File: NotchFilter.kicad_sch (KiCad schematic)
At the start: 10 parts, among them U4 LM2904DR

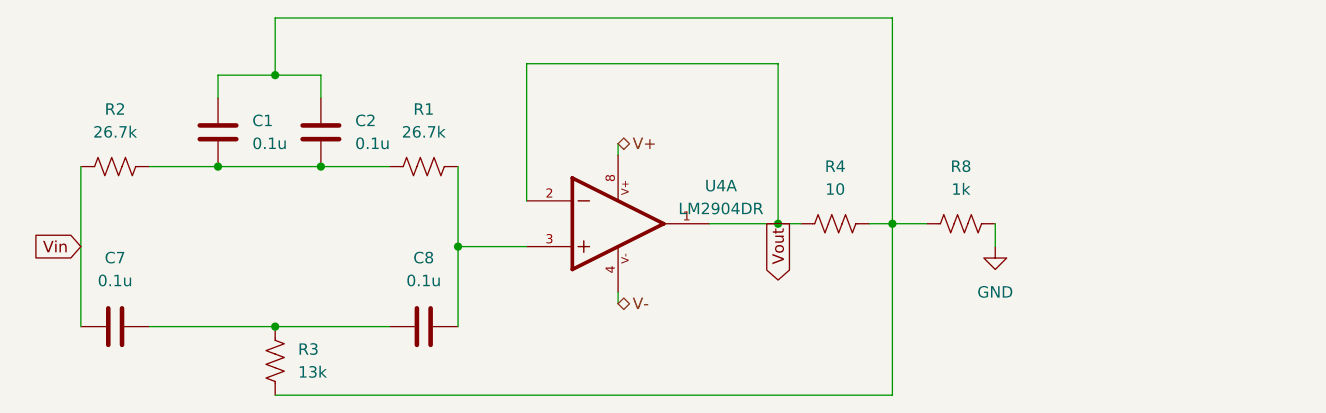
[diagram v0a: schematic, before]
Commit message: swapped lpf and hpf in bandpass filter and added testpoints on various filter circuits
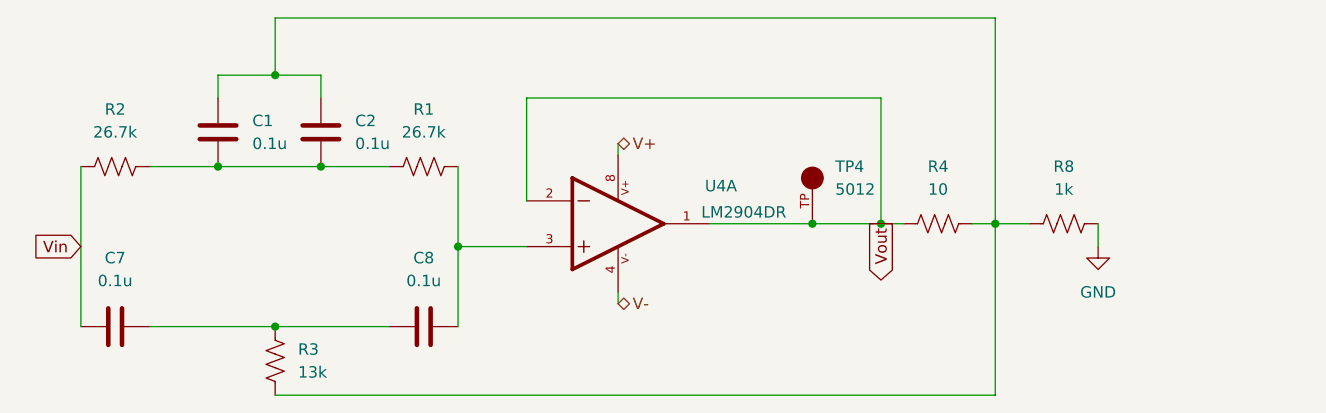
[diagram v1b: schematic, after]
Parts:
- added TP4: 5012, 5012:TP_5012, symbol TP_5012:5012
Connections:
- net Vout: now also TP4.TP
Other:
- moved on the sheet: R4, R8
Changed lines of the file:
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@@
 (kicad_sch (version 20230121) (generator eeschema)
   (paper "A4")
+  (junction (at 209.55 77.47) (diameter 0) (color 0 0 0 0)
+  )
+  (junction (at 162.56 80.01) (diameter 0) (color 0 0 0 0)
+  )
   (junction (at 142.24 60.96) (diameter 0) (color 0 0 0 0)
   )
-  (junction (at 198.12 77.47) (diameter 0) (color 0 0 0 0)
-  )
-  (junction (at 162.56 80.01) (diameter 0) (color 0 0 0 0)
-  )
   (junction (at 135.89 71.12) (diameter 0) (color 0 0 0 0)
   )
-  (junction (at 210.82 77.47) (diameter 0) (color 0 0 0 0)
+  (junction (at 222.25 77.47) (diameter 0) (color 0 0 0 0)
+  )
+  (junction (at 201.93 77.47) (diameter 0) (color 0 0 0 0)
   )
   (junction (at 147.32 71.12) (diameter 0) (color 0 0 0 0)
@@
     (stroke (width 0) (type default))
   )
-  (wire (pts (xy 170.18 59.69) (xy 198.12 59.69))
+  (wire (pts (xy 170.18 63.5) (xy 209.55 63.5))
     (stroke (width 0) (type default))
   )
@@
     (stroke (width 0) (type default))
   )
-  (wire (pts (xy 142.24 96.52) (xy 210.82 96.52))
+  (wire (pts (xy 201.93 77.47) (xy 209.55 77.47))
     (stroke (width 0) (type default))
   )
@@
     (stroke (width 0) (type default))
   )
+  (wire (pts (xy 135.89 60.96) (xy 142.24 60.96))
+    (stroke (width 0) (type default))
+  )
   (wire (pts (xy 162.56 80.01) (xy 162.56 88.9))
     (stroke (width 0) (type default))
   )
+  (wire (pts (xy 170.18 63.5) (xy 170.18 74.93))
+    (stroke (width 0) (type default))
+  )
   (wire (pts (xy 142.24 54.61) (xy 142.24 60.96))
     (stroke (width 0) (type default))
   )
-  (wire (pts (xy 190.5 77.47) (xy 198.12 77.47))
-    (stroke (width 0) (type default))
-  )
   (wire (pts (xy 162.56 71.12) (xy 162.56 80.01))
     (stroke (width 0) (type default))
@@
     (stroke (width 0) (type default))
   )
-  (wire (pts (xy 222.25 77.47) (xy 222.25 80.01))
+  (wire (pts (xy 233.68 77.47) (xy 233.68 80.01))
     (stroke (width 0) (type default))
   )
@@
     (stroke (width 0) (type default))
   )
-  (wire (pts (xy 210.82 77.47) (xy 214.63 77.47))
-    (stroke (width 0) (type default))
-  )
-  (wire (pts (xy 170.18 74.93) (xy 170.18 59.69))
-    (stroke (width 0) (type default))
-  )
-  (wire (pts (xy 210.82 54.61) (xy 142.24 54.61))
+  (wire (pts (xy 222.25 77.47) (xy 226.06 77.47))
+    (stroke (width 0) (type default))
+  )
+  (wire (pts (xy 222.25 54.61) (xy 142.24 54.61))
     (stroke (width 0) (type default))
   )
@@
     (stroke (width 0) (type default))
   )
+  (wire (pts (xy 190.5 77.47) (xy 201.93 77.47))
+    (stroke (width 0) (type default))
+  )
   (wire (pts (xy 147.32 71.12) (xy 154.94 71.12))
     (stroke (width 0) (type default))
   )
-  (wire (pts (xy 135.89 60.96) (xy 142.24 60.96))
-    (stroke (width 0) (type default))
-  )
-  (wire (pts (xy 208.28 77.47) (xy 210.82 77.47))
+  (wire (pts (xy 219.71 77.47) (xy 222.25 77.47))
+    (stroke (width 0) (type default))
+  )
+  (wire (pts (xy 222.25 77.47) (xy 222.25 54.61))
     (stroke (width 0) (type default))
   )
@@
     (stroke (width 0) (type default))
   )
-  (wire (pts (xy 210.82 77.47) (xy 210.82 54.61))
-    (stroke (width 0) (type default))
-  )
   (wire (pts (xy 180.34 85.09) (xy 180.34 86.36))
     (stroke (width 0) (type default))
   )
-  (wire (pts (xy 198.12 77.47) (xy 200.66 77.47))
-    (stroke (width 0) (type default))
-  )
-  (wire (pts (xy 210.82 77.47) (xy 210.82 96.52))
-    (stroke (width 0) (type default))
-  )
-  (wire (pts (xy 198.12 59.69) (xy 198.12 77.47))
+  (wire (pts (xy 142.24 96.52) (xy 222.25 96.52))
+    (stroke (width 0) (type default))
+  )
+  (wire (pts (xy 209.55 77.47) (xy 212.09 77.47))
+    (stroke (width 0) (type default))
+  )
+  (wire (pts (xy 222.25 77.47) (xy 222.25 96.52))
+    (stroke (width 0) (type default))
+  )
+  (wire (pts (xy 209.55 63.5) (xy 209.55 77.47))
     (stroke (width 0) (type default))
   )
@@
     (stroke (width 0) (type default))
   )
-  (global_label "Vout" (shape output) (at 198.12 77.47 270) (fields_autoplaced)
+  (global_label "Vout" (shape output) (at 209.55 77.47 270) (fields_autoplaced)
     (effects (font (size 1.27 1.27)) (justify right))
-    (property "Intersheetrefs" "${INTERSHEET_REFS}" (at 198.12 84.5675 90)
+    (property "Intersheetrefs" "${INTERSHEET_REFS}" (at 209.55 84.5675 90)
       (effects (font (size 1.27 1.27)) (justify right) hide)
     )
@@
   )
   (symbol (lib_id "LM2904DR:LM2904DR") (at 180.34 77.47 0) (unit 1)
-    (in_bom yes) (on_board yes) (dnp no) (fields_autoplaced)
+    (in_bom yes) (on_board yes) (dnp no)
     (property "Reference" "U4" (at 191.77 73.2791 0)
       (effects (font (size 1.27 1.27)))
     )
-    (property "Value" "LM2904DR" (at 191.77 75.8191 0)
+    (property "Value" "LM2904DR" (at 194.31 76.2 0)
       (effects (font (size 1.27 1.27)))
     )
@@
     )
   )
-  (symbol (lib_id "power:GND") (at 222.25 80.01 0) (unit 1)
-    (in_bom yes) (on_board yes) (dnp no) (fields_autoplaced)
-    (property "Reference" "#PWR02" (at 222.25 86.36 0)
-      (effects (font (size 1.27 1.27)) hide)
-    )
-    (property "Value" "GND" (at 222.25 85.09 0)
-      (effects (font (size 1.27 1.27)))
-    )
-    (property "Footprint" "" (at 222.25 80.01 0)
-      (effects (font (size 1.27 1.27)) hide)
-    )
-    (property "Datasheet" "" (at 222.25 80.01 0)
+  (symbol (lib_id "power:GND") (at 233.68 80.01 0) (unit 1)
+    (in_bom yes) (on_board yes) (dnp no) (fields_autoplaced)
+    (property "Reference" "#PWR02" (at 233.68 86.36 0)
+      (effects (font (size 1.27 1.27)) hide)
+    )
+    (property "Value" "GND" (at 233.68 85.09 0)
+      (effects (font (size 1.27 1.27)))
+    )
+    (property "Footprint" "" (at 233.68 80.01 0)
+      (effects (font (size 1.27 1.27)) hide)
+    )
+    (property "Datasheet" "" (at 233.68 80.01 0)
       (effects (font (size 1.27 1.27)) hide)
     )
@@
         (path "/c6167f6f-8a8c-40a1-9c06-7f0e8ea44639/7fb3b184-acaf-47e3-98f1-99223ca2f08b"
           (reference "C7") (unit 1)
+        )
+      )
+    )
+  )
+  (symbol (lib_id "TP_5012:5012") (at 201.93 72.39 90) (unit 1)
+    (in_bom yes) (on_board yes) (dnp no) (fields_autoplaced)
+    (property "Reference" "TP4" (at 204.47 71.12 90)
+      (effects (font (size 1.27 1.27)) (justify right))
+    )
+    (property "Value" "5012" (at 204.47 73.66 90)
+      (effects (font (size 1.27 1.27)) (justify right))
+    )
+    (property "Footprint" "5012:TP_5012" (at 201.93 72.39 0)
+      (effects (font (size 1.27 1.27)) (justify bottom) hide)
+    )
+    (property "Datasheet" "" (at 201.93 72.39 0)
+      (effects (font (size 1.27 1.27)) hide)
+    )
+    (property "PARTREV" "F" (at 201.93 72.39 0)
+      (effects (font (size 1.27 1.27)) (justify bottom) hide)
+    )
+    (property "SNAPEDA_PN" "5010" (at 201.93 72.39 0)
+      (effects (font (size 1.27 1.27)) (justify bottom) hide)
+    )
+    (property "MANUFACTURER" "Keystone Electronics" (at 201.93 72.39 0)
+      (effects (font (size 1.27 1.27)) (justify bottom) hide)
+    )
+    (property "MAXIMUM_PACKAGE_HEIGHT" "8.13 mm" (at 201.93 72.39 0)
+      (effects (font (size 1.27 1.27)) (justify bottom) hide)
+    )
+    (property "STANDARD" "Manufacturer Recommendations" (at 201.93 72.39 0)
+      (effects (font (size 1.27 1.27)) (justify bottom) hide)
+    )
+    (pin "TP")
+    (instances
+      (project "TR_EMG"
+        (path "/c6167f6f-8a8c-40a1-9c06-7f0e8ea44639/7fb3b184-acaf-47e3-98f1-99223ca2f08b"
+          (reference "TP4") (unit 1)
         )
       )
@@
     )
   )
-  (symbol (lib_id "Device:R_US") (at 218.44 77.47 270) (unit 1)
-    (in_bom yes) (on_board yes) (dnp no) (fields_autoplaced)
-    (property "Reference" "R8" (at 218.44 71.12 90)
-      (effects (font (size 1.27 1.27)))
-    )
-    (property "Value" "1k" (at 218.44 73.66 90)
-      (effects (font (size 1.27 1.27)))
-    )
-    (property "Footprint" "" (at 218.186 78.486 90)
-      (effects (font (size 1.27 1.27)) hide)
-    )
-    (property "Datasheet" "~" (at 218.44 77.47 0)
+  (symbol (lib_id "Device:R_US") (at 229.87 77.47 270) (unit 1)
+    (in_bom yes) (on_board yes) (dnp no) (fields_autoplaced)
+    (property "Reference" "R8" (at 229.87 71.12 90)
+      (effects (font (size 1.27 1.27)))
+    )
+    (property "Value" "1k" (at 229.87 73.66 90)
+      (effects (font (size 1.27 1.27)))
+    )
+    (property "Footprint" "" (at 229.616 78.486 90)
+      (effects (font (size 1.27 1.27)) hide)
+    )
+    (property "Datasheet" "~" (at 229.87 77.47 0)
       (effects (font (size 1.27 1.27)) hide)
     )
@@
     )
   )
-  (symbol (lib_id "Device:R_US") (at 204.47 77.47 270) (unit 1)
-    (in_bom yes) (on_board yes) (dnp no) (fields_autoplaced)
-    (property "Reference" "R4" (at 204.47 71.12 90)
-      (effects (font (size 1.27 1.27)))
-    )
-    (property "Value" "10" (at 204.47 73.66 90)
-      (effects (font (size 1.27 1.27)))
-    )
-    (property "Footprint" "" (at 204.216 78.486 90)
-      (effects (font (size 1.27 1.27)) hide)
-    )
-    (property "Datasheet" "~" (at 204.47 77.47 0)
-      (effects (font (size 1.27 1.27)) hide)
-    )
+  (symbol (lib_id "Device:R_US") (at 215.9 77.47 270) (unit 1)
+    (in_bom yes) (on_board yes) (dnp no) (fields_autoplaced)
+    (property "Reference" "R4" (at 215.9 71.12 90)
+      (effects (font (size 1.27 1.27)))
+    )
+    (property "Value" "10" (at 215.9 73.66 90)
+      (effects (font (size 1.27 1.27)))
+    )
+    (property "Footprint" "" (at 215.646 78.486 90)
+      (effects (font (size 1.27 1.27)) hide)
+    )
+    (property "Datasheet" "~" (at 215.9 77.47 0)
+      (effects (font (size 1.27 1.27)) hide)
+    )

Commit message: merge fix 2
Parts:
- removed U4: LM2904DR, LM2904DR:SOIC127P599X175-8N, symbol LM2904DR:LM2904DR
- added U2: LT1169CS8-PBF, SO-8_S_LIT, symbol symbols:LT1169CS8-PBF
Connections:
- net V+: now also U2.8 (V+)
- net V-: now also U2.4 (V-)
- net Vout: now also U2.1 (OUTA), U2.2 (-INA)
- net at C8.2, R1.2: now also U2.3 (+INA)
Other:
- moved on the sheet: R4, R8, TP4

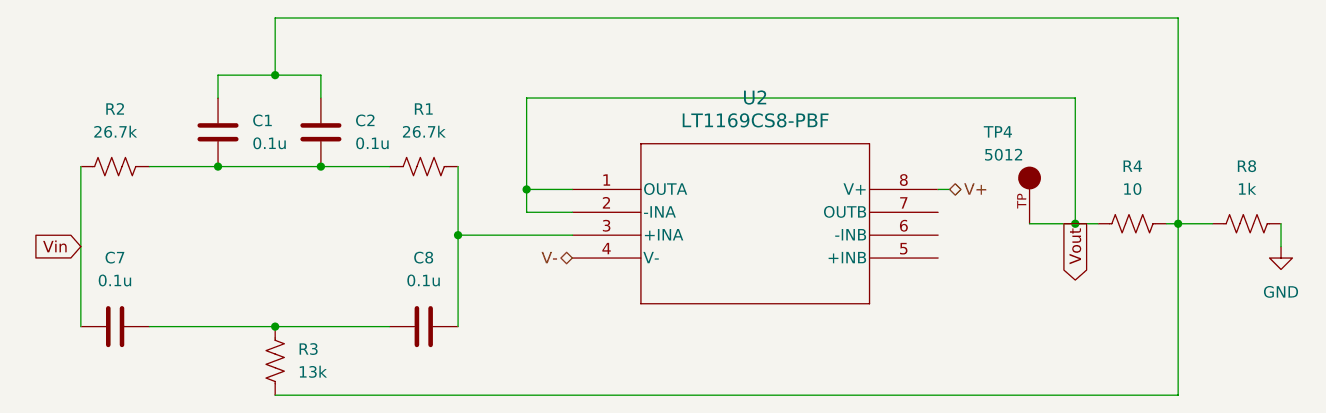
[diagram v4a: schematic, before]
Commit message: Reference Designator and Footprint Updates
Changed almost all reference designators to group similar components by what filter they are a part of and what value they have.

Need to:
- Sort symbol data for ADC and OpAmps to correct folders
- get footprint files for ADC and OpAmps
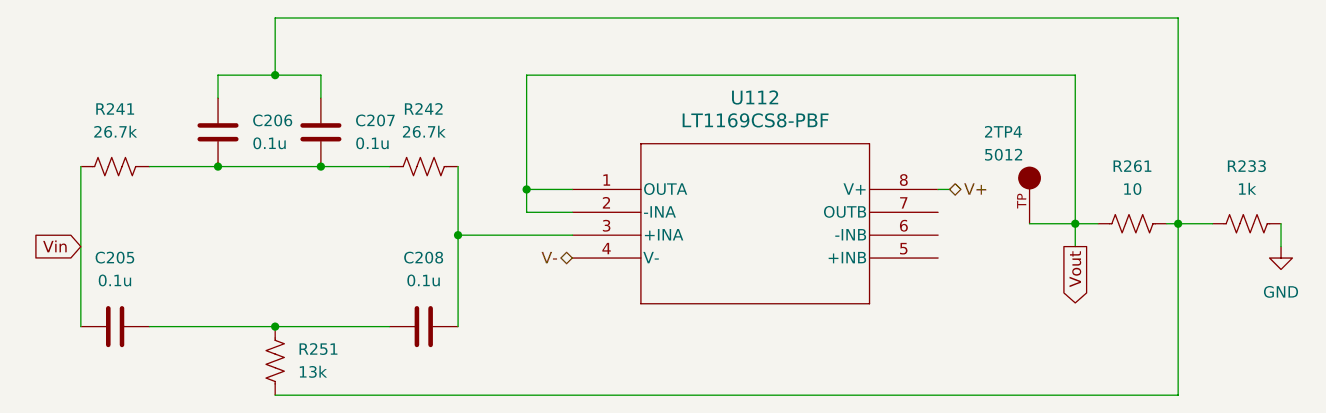
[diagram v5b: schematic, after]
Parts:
- 2TP4: renamed from TP4; footprint 5012:TP_5012 -> footprints:TP_5012
- C205: renamed from C7; footprint (none) -> Capacitor_SMD:C_0603_1608Metric_Pad1.08x0.95mm_HandSolder
- C206: renamed from C1; footprint (none) -> Capacitor_SMD:C_0603_1608Metric_Pad1.08x0.95mm_HandSolder
- C207: renamed from C2; footprint (none) -> Capacitor_SMD:C_0603_1608Metric_Pad1.08x0.95mm_HandSolder
- C208: renamed from C8; footprint (none) -> Capacitor_SMD:C_0603_1608Metric_Pad1.08x0.95mm_HandSolder
- R233: renamed from R8; footprint (none) -> Resistor_SMD:R_0603_1608Metric_Pad0.98x0.95mm_HandSolder
- R241: renamed from R2; footprint (none) -> Resistor_SMD:R_0603_1608Metric_Pad0.98x0.95mm_HandSolder
- R242: renamed from R1; footprint (none) -> Resistor_SMD:R_0603_1608Metric_Pad0.98x0.95mm_HandSolder
- R251: renamed from R3; footprint (none) -> Resistor_SMD:R_0603_1608Metric_Pad0.98x0.95mm_HandSolder
- R261: renamed from R4; footprint (none) -> Resistor_SMD:R_0603_1608Metric_Pad0.98x0.95mm_HandSolder
- U112: renamed from U2; footprint SO-8_S_LIT -> footprints:SOIC127P599X175-8N

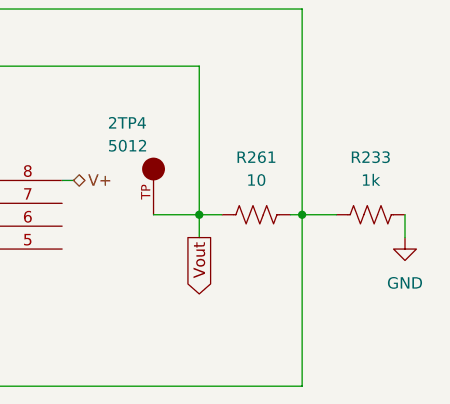
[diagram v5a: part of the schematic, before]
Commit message: updated GND symbols for appropriate seperatiion of analog and digital grounds
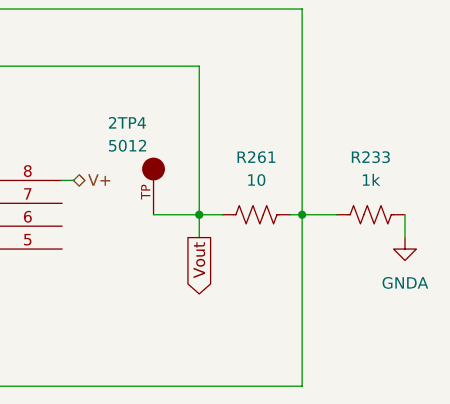
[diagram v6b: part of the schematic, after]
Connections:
- net GND renamed GNDA
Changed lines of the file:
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@@
-    )
-  )
-  (symbol (lib_id "power:GND") (at 254 80.01 0) (unit 1)
-    (in_bom yes) (on_board yes) (dnp no) (fields_autoplaced)
-    (property "Reference" "#PWR0103" (at 254 86.36 0)
-      (effects (font (size 1.27 1.27)) hide)
-    )
-    (property "Value" "GND" (at 254 85.09 0)
-      (effects (font (size 1.27 1.27)))
-    )
-    (property "Footprint" "" (at 254 80.01 0)
-      (effects (font (size 1.27 1.27)) hide)
-    )
-    (property "Datasheet" "" (at 254 80.01 0)
-      (effects (font (size 1.27 1.27)) hide)
-    )
-    (pin "1")
-    (instances
-      (project "TR_EMG"
-        (path "/c6167f6f-8a8c-40a1-9c06-7f0e8ea44639/e619882c-69e2-4357-9513-12f0ec23e799/2f0a58c0-1c44-4e98-afee-bedece3a8259"
-          (reference "#PWR0103") (unit 1)
-        )
-        (path "/c6167f6f-8a8c-40a1-9c06-7f0e8ea44639/a0268632-eb9a-430e-97ab-e20adbf6cd41/2f0a58c0-1c44-4e98-afee-bedece3a8259"
-          (reference "#PWR02") (unit 1)
-        )
-        (path "/c6167f6f-8a8c-40a1-9c06-7f0e8ea44639/1e802adc-784c-4bfc-ac56-2ca34eafc640/2f0a58c0-1c44-4e98-afee-bedece3a8259"
-          (reference "#PWR0106") (unit 1)
-        )
-        (path "/c6167f6f-8a8c-40a1-9c06-7f0e8ea44639/fca8234f-eea0-4615-81d1-2ac2d4337d1e/2f0a58c0-1c44-4e98-afee-bedece3a8259"
-          (reference "#PWR0109") (unit 1)
-        )
-      )
     )
   )
@@
         )
       )
+    )
+  )
+  (symbol (lib_id "power:GNDA") (at 254 80.01 0) (unit 1)
+    (in_bom yes) (on_board yes) (dnp no) (fields_autoplaced)
+    (property "Reference" "#PWR02" (at 254 86.36 0)
+      (effects (font (size 1.27 1.27)) hide)
+    )
+    (property "Value" "GNDA" (at 254 85.09 0)
+      (effects (font (size 1.27 1.27)))
+    )
+    (property "Footprint" "" (at 254 80.01 0)
+      (effects (font (size 1.27 1.27)) hide)
+    )
+    (property "Datasheet" "" (at 254 80.01 0)
+      (effects (font (size 1.27 1.27)) hide)
+    )
+    (pin "1")
+    (instances
+      (project "TR_EMG"
+        (path "/c6167f6f-8a8c-40a1-9c06-7f0e8ea44639/a0268632-eb9a-430e-97ab-e20adbf6cd41/2f0a58c0-1c44-4e98-afee-bedece3a8259"
+          (reference "#PWR02") (unit 1)
+        )
+        (path "/c6167f6f-8a8c-40a1-9c06-7f0e8ea44639/e619882c-69e2-4357-9513-12f0ec23e799/2f0a58c0-1c44-4e98-afee-bedece3a8259"
+          (reference "#PWR011") (unit 1)
+        )
+        (path "/c6167f6f-8a8c-40a1-9c06-7f0e8ea44639/1e802adc-784c-4bfc-ac56-2ca34eafc640/2f0a58c0-1c44-4e98-afee-bedece3a8259"
+          (reference "#PWR012") (unit 1)
+        )
+        (path "/c6167f6f-8a8c-40a1-9c06-7f0e8ea44639/fca8234f-eea0-4615-81d1-2ac2d4337d1e/2f0a58c0-1c44-4e98-afee-bedece3a8259"
+          (reference "#PWR013") (unit 1)
+        )
+      )

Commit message: renamed and relinked footprints with better clarity footprint file names
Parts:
- U112: footprint footprints:SOIC127P599X175-8N -> footprints:LT-SOIC127P599X175-8N
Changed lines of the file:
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@@
       (effects (font (size 1.524 1.524)))
     )
-    (property "Footprint" "footprints:SOIC127P599X175-8N" (at 175.26 73.66 0)
+    (property "Footprint" "footprints:LT-SOIC127P599X175-8N" (at 175.26 73.66 0)
       (effects (font (size 1.27 1.27) italic) hide)
     )

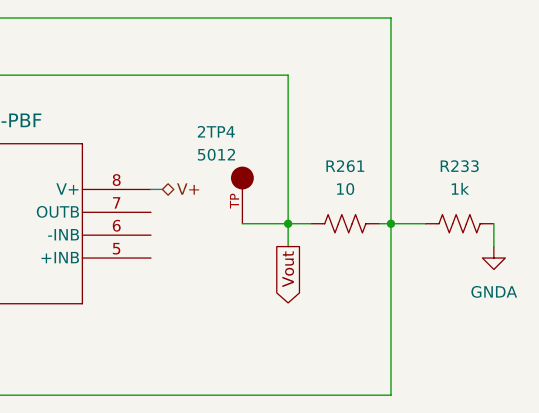
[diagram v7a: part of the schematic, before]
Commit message: final adjustments for power constraints with changed footprint and resistor values on notch filter feedback portion
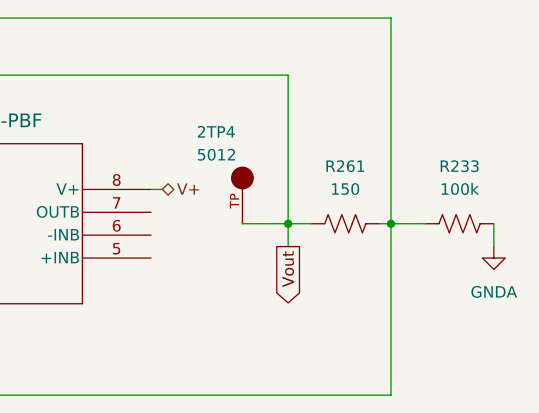
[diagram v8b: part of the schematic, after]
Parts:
- R233: value 1k -> 100k
- R261: value 10 -> 150; footprint Resistor_SMD:R_0603_1608Metric_Pad0.98x0.95mm_HandSolder -> Resistor_SMD:R_2010_5025Metric
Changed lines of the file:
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@@
       (effects (font (size 1.27 1.27)))
     )
-    (property "Value" "1k" (at 250.19 73.66 90)
+    (property "Value" "100k" (at 250.19 73.66 90)
       (effects (font (size 1.27 1.27)))
     )
@@
       (effects (font (size 1.27 1.27)))
     )
-    (property "Value" "10" (at 237.49 73.66 90)
+    (property "Value" "150" (at 237.49 73.66 90)
       (effects (font (size 1.27 1.27)))
     )
-    (property "Footprint" "Resistor_SMD:R_0603_1608Metric_Pad0.98x0.95mm_HandSolder" (at 237.236 78.486 90)
+    (property "Footprint" "Resistor_SMD:R_2010_5025Metric" (at 237.236 78.486 90)
       (effects (font (size 1.27 1.27)) hide)
     )
